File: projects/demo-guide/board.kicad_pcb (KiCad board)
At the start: 2 copper layers, 100 x 100 mm, 5 parts

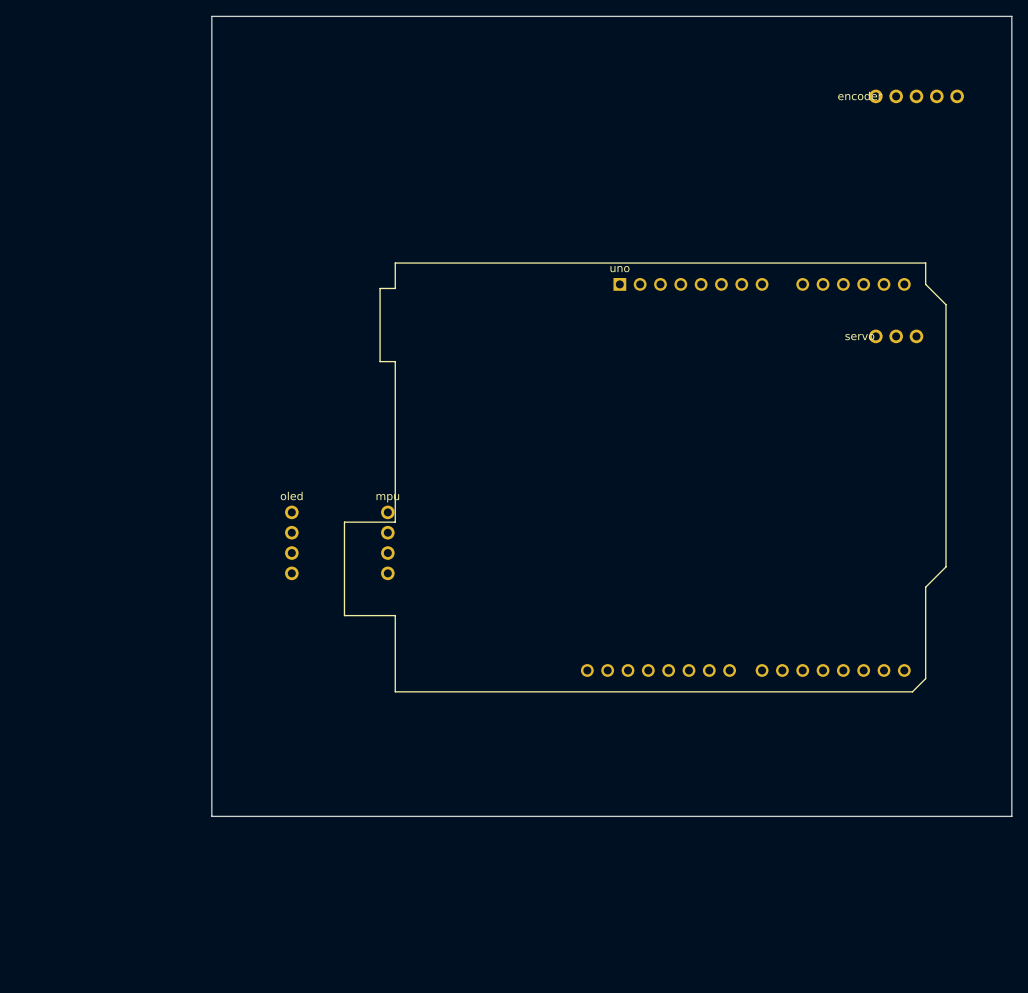
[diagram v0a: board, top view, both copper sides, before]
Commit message: Add landing page, demo-guide project, DeepPCB integration, and UI fixes
- Redesign landing page to match editor aesthetic (toolbar, tabs, monospace)
- Add demo-guide project with interactive walkthrough and PCB layout
- Add project metadata API (part count, types, line count, PCB/test badges)
- Add DeepPCB autorouter API integration
- Fix logo spacing in editor toolbar
- Improve PCB editor drag, sexpr mutations, and simulation panel
- Update Sparky prompts and chat API

Co-Authored-By: Claude Opus 4.6 <noreply@anthropic.com>
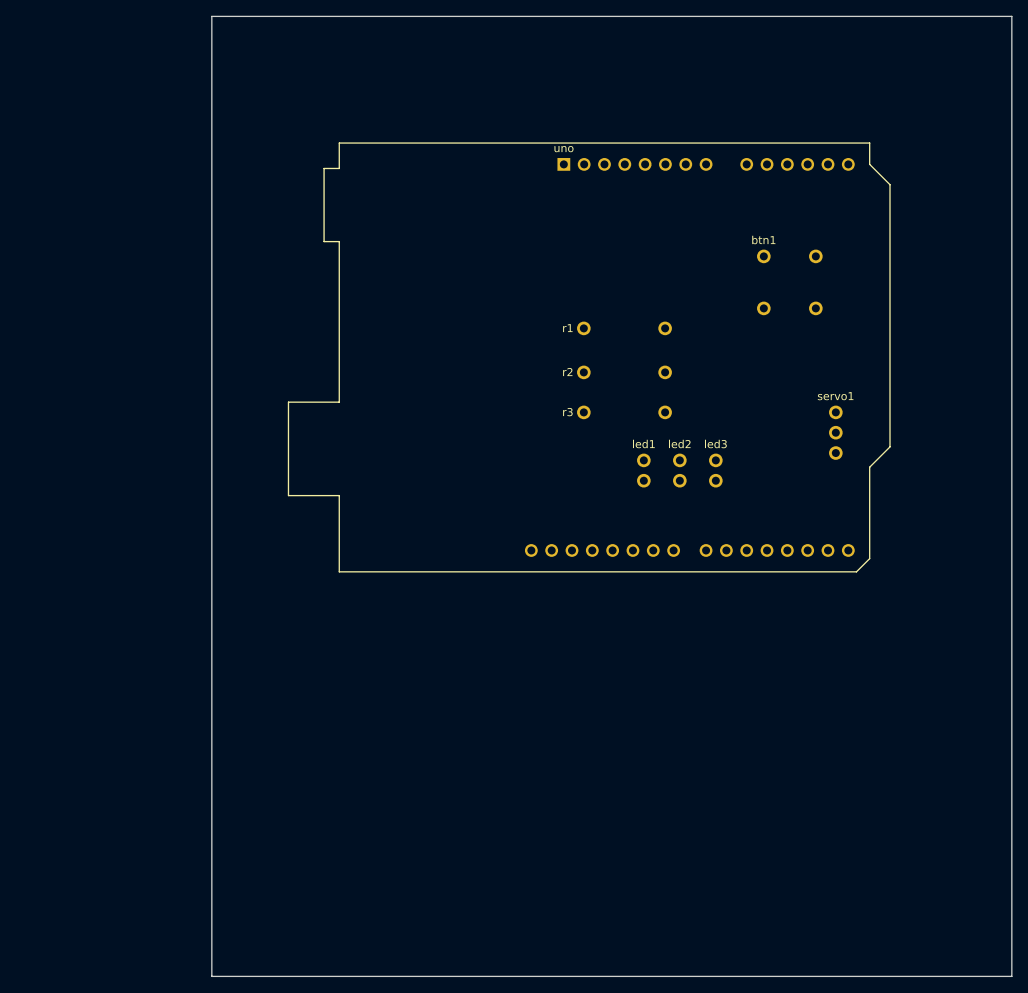
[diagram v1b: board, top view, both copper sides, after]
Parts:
- removed encoder: KY-040 Encoder, Header-1x05
- removed mpu: MPU6050, Header-1x04
- removed oled: SSD1306 OLED, Header-1x04
- removed servo: Servo, Header-1x03
- added btn1: SW-THT-6mm, SW-THT-6mm, F.Cu at (69.0, 30.0)
- added led1: LED-THT-3mm, LED-THT-3mm, F.Cu at (54.0, 55.5)
- added led2: LED-THT-3mm, LED-THT-3mm, F.Cu at (58.5, 55.5)
- added led3: LED-THT-3mm, LED-THT-3mm, F.Cu at (63.0, 55.5)
- added r1: 220, Axial-0.4in, F.Cu at (46.5, 39.0)
- added r2: 220, Axial-0.4in, F.Cu at (46.5, 44.5)
- added r3: 220, Axial-0.4in, F.Cu at (46.5, 49.5)
- added servo1: Header-1x3, Header-1x3, F.Cu at (78.0, 49.5)
- moved uno 16.6 mm to (44.0, 18.5)
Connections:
- uno pad uno:11: (no net) -> Net-6
- uno pad uno:12: (no net) -> Net-4
- uno pad uno:13: (no net) -> Net-1
- uno pad uno:2: Net-5 -> Net-8
- uno pad uno:3: Net-6 -> (no net)
- uno pad uno:4: Net-7 -> (no net)
- uno pad uno:5V: Net-3 -> Net-11
- uno pad uno:9: Net-9 -> Net-13
- uno pad uno:A0: (no net) -> Net-10
- uno pad uno:A4: Net-1 -> (no net)
- uno pad uno:A5: Net-2 -> (no net)
- uno pad uno:GND.1: Net-8 -> Net-3
- uno pad uno:GND.2: Net-4 -> Net-9
- uno pad uno:GND.3: Net-10 -> Net-12
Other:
- board size 100 x 100 mm -> 100 x 120 mm

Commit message: Regenerate demo-guide board.kicad_pcb with net assignments
The on-disk board file was generated before the pin name mapping
fix, so all pads had no nets. Regenerated to include proper net
assignments so ratsnest displays immediately without needing to
click "Update from Diagram".

Co-Authored-By: Claude Opus 4.6 <noreply@anthropic.com>
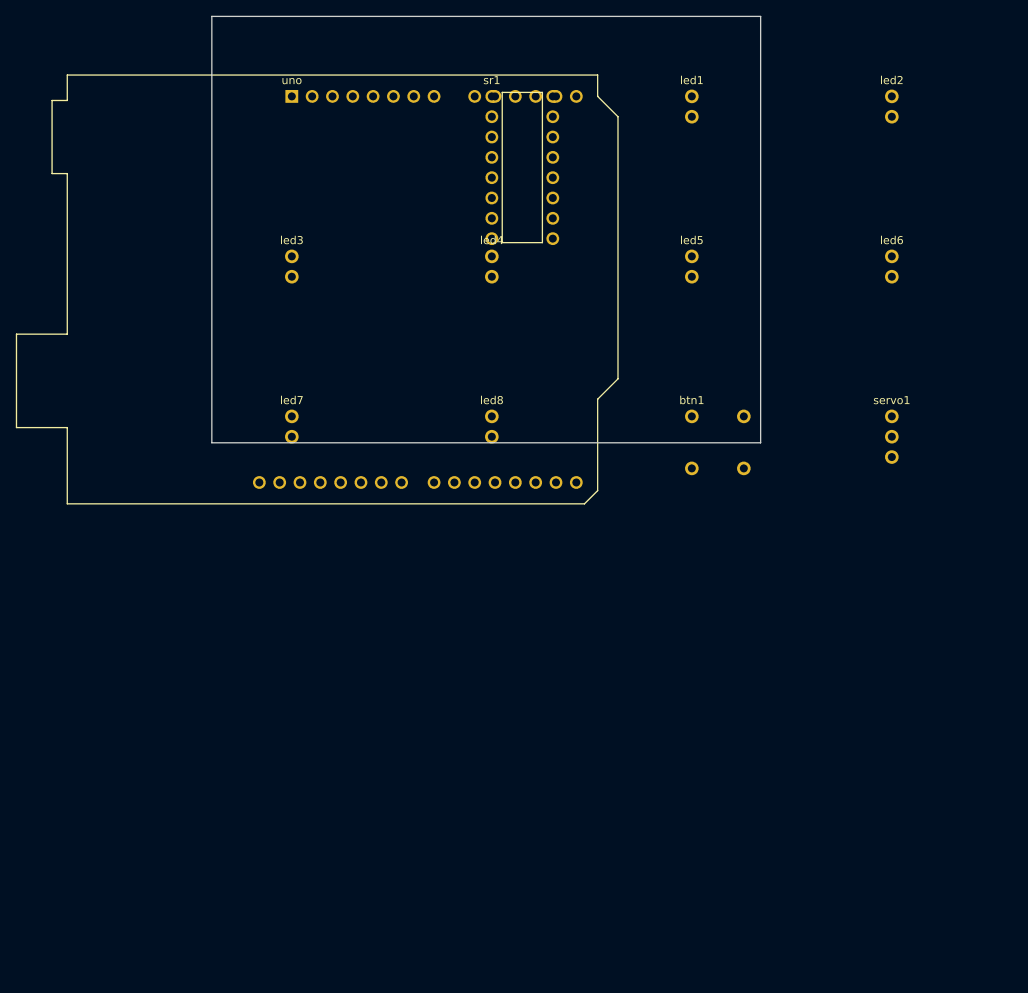
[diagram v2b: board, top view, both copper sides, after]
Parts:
- removed r1, r2, r3: 220, Axial-0.4in
- added led4: LED-THT-3mm, LED-THT-3mm, F.Cu at (35.0, 30.0)
- added led5: LED-THT-3mm, LED-THT-3mm, F.Cu at (60.0, 30.0)
- added led6: LED-THT-3mm, LED-THT-3mm, F.Cu at (85.0, 30.0)
- added led7: LED-THT-3mm, LED-THT-3mm, F.Cu at (10.0, 50.0)
- added led8: LED-THT-3mm, LED-THT-3mm, F.Cu at (35.0, 50.0)
- added sr1: DIP-16, DIP-16, F.Cu at (35.0, 10.0)
- moved led3 58.8 mm to (10.0, 30.0)
- moved led2 52.7 mm to (85.0, 10.0)
- moved led1 45.9 mm to (60.0, 10.0)
- moved uno 35.0 mm to (10.0, 10.0)
- moved btn1 21.9 mm to (60.0, 50.0)
- moved servo1 7.02 mm to (85.0, 50.0)
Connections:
- net Net-10 renamed Net-16
- btn1 pad btn1:1: (no net) -> Net-15
- btn1 pad btn1:4: (no net) -> Net-14
- led1 pad led1:1: (no net) -> Net-6
- led1 pad led1:2: (no net) -> Net-5
- led2 pad led2:1: (no net) -> Net-7
- led2 pad led2:2: (no net) -> Net-5
- led3 pad led3:1: (no net) -> Net-8
- led3 pad led3:2: (no net) -> Net-5
- servo1 pad servo1:1: (no net) -> Net-17
- servo1 pad servo1:2: (no net) -> Net-4
- servo1 pad servo1:3: (no net) -> Net-18
- uno pad uno:11: Net-6 -> (no net)
- uno pad uno:12: Net-4 -> (no net)
- uno pad uno:13: Net-1 -> (no net)
- uno pad uno:2: Net-8 -> Net-1
- uno pad uno:3: (no net) -> Net-2
- uno pad uno:4: (no net) -> Net-3
- uno pad uno:5: (no net) -> Net-14
- uno pad uno:5V: Net-11 -> Net-4
- uno pad uno:9: Net-13 -> Net-18
- uno pad uno:GND.1: Net-3 -> Net-5
- uno pad uno:GND.2: Net-9 -> Net-15
- uno pad uno:GND.3: Net-12 -> Net-17
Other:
- board size 100 x 120 mm -> 68.6 x 53.3 mm

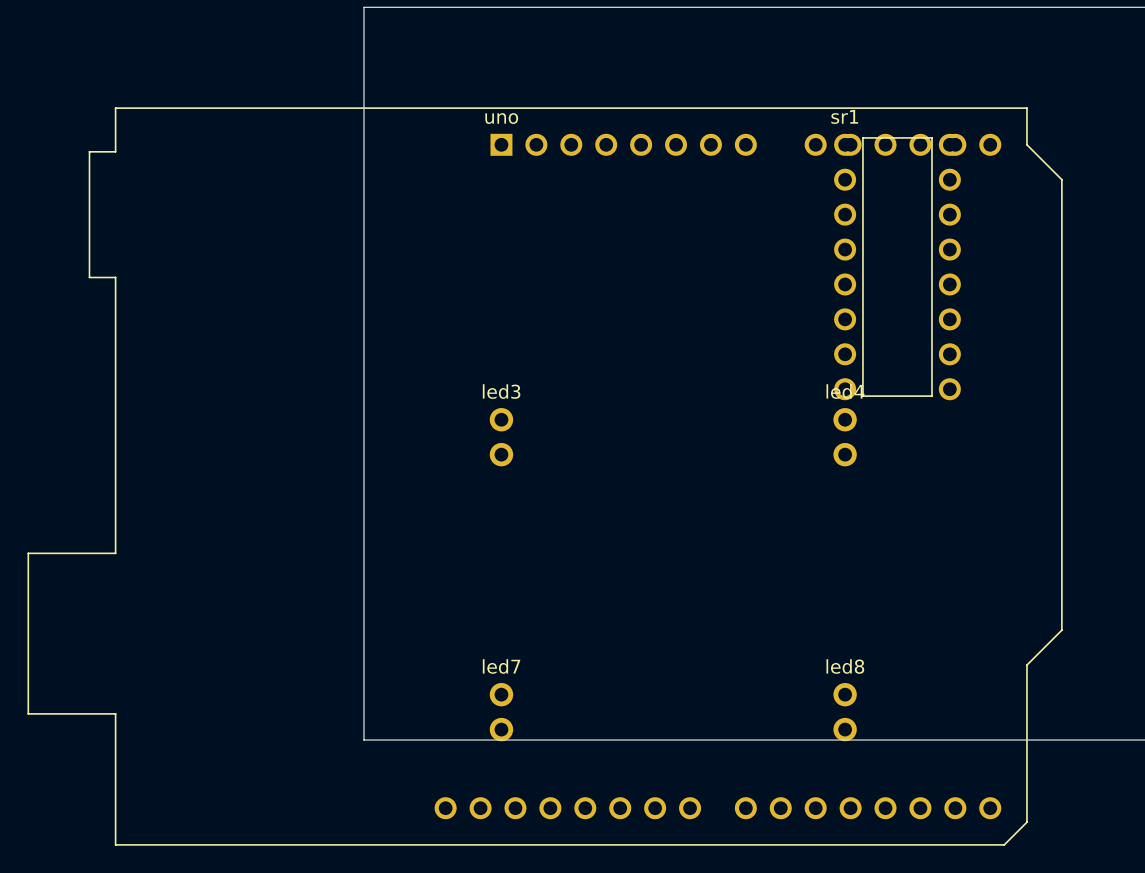
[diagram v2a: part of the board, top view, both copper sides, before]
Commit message: Add PCB trace routing, via placement, and wire/diagram improvements
- Wire useKiPCBRouting hook into KiPCBEditor for interactive trace routing (X) and via placement (V)
- Add segment/via S-expression builders and net number resolver to sexpr-mutate
- Rewrite routing hook to work with S-expr trees: click-pad-to-start, waypoints, rubber-band preview
- JLC-compatible sizes: 0.25mm trace, 0.8mm via diameter, 0.4mm drill
- Fix demo-guide diagram wiring to avoid component overlap
- Update demo-guide board and outline

Co-Authored-By: Claude Opus 4.6 <noreply@anthropic.com>
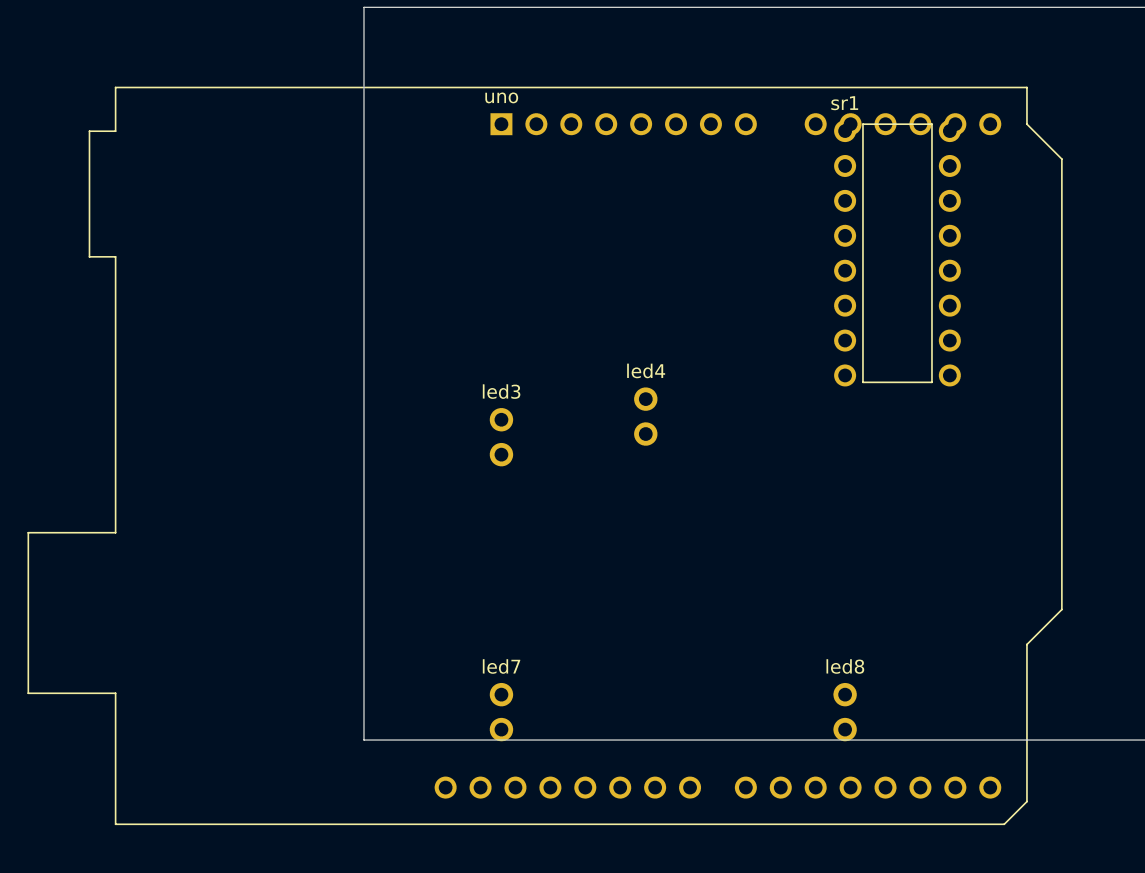
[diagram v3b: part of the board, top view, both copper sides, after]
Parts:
- moved led4 14.6 mm to (20.5, 28.5)
- moved uno 1.50 mm to (10.0, 8.50)
- moved sr1 1.00 mm to (35.0, 9.00)
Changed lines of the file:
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@@
   (footprint Arduino-Uno-Shield
     (layer F.Cu)
-    (at 10 10)
+    (at 10 8.5 0)
     (attr through_hole)
     (fp_text reference uno
@@
   (footprint DIP-16
     (layer F.Cu)
-    (at 35 10)
+    (at 35 9 0)
     (attr through_hole)
     (fp_text reference sr1
@@
   (footprint LED-THT-3mm
     (layer F.Cu)
-    (at 35 30)
+    (at 20.5 28.5 0)
     (attr through_hole)
     (fp_text reference led4
